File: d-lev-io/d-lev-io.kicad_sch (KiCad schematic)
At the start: 29 parts, among them J1 PJ-059A, J2 USB_C_Receptacle_USB2.0, J8 Conn_01x12_MountingPin, U1 AMS1117-ADJ

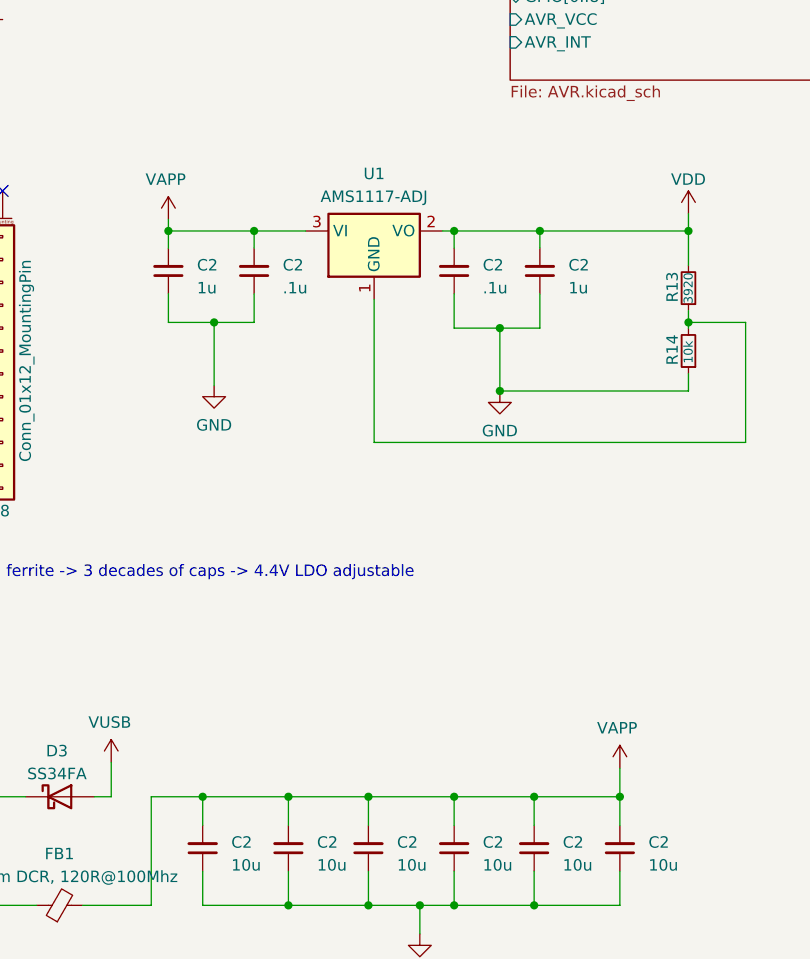
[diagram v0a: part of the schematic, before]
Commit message: mostly done routing
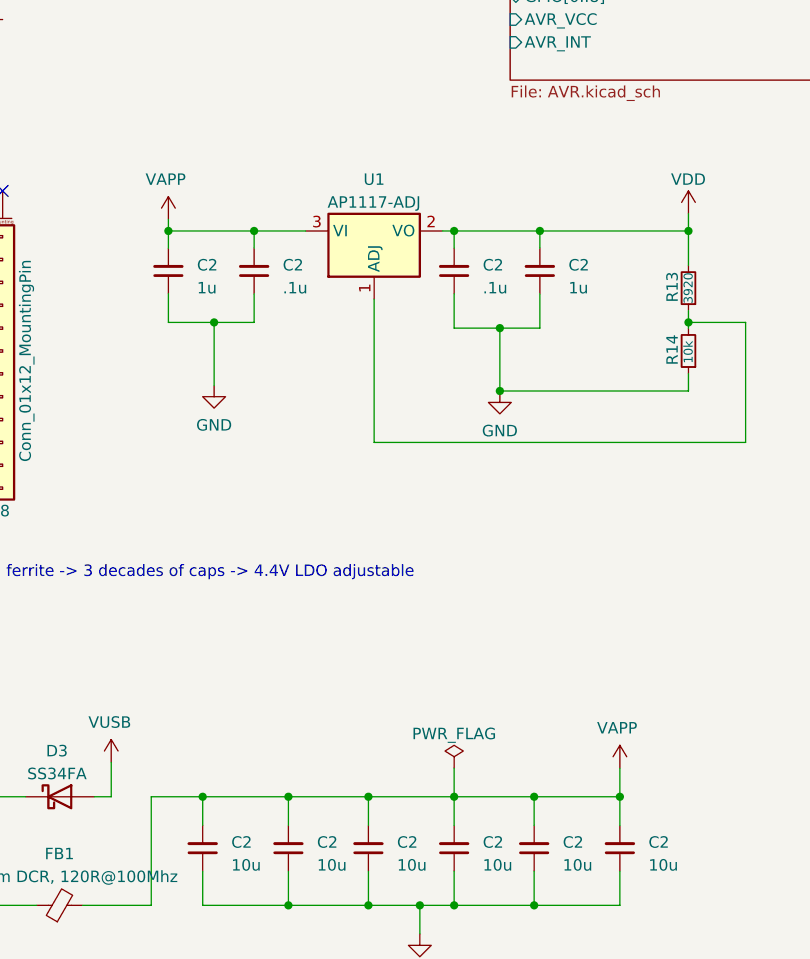
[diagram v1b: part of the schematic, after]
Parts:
- removed U1: AMS1117-ADJ, Package_TO_SOT_SMD:SOT-223-3_TabPin2, symbol Regulator_Linear:AMS1117-5.0
- added U1: AP1117-ADJ, Package_TO_SOT_SMD:SOT-223-3_TabPin2, symbol Regulator_Linear:AP1117-ADJ
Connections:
- net +5V: now also U1.2 (VO)
- net VBUS: now also U1.3 (VI)
- net at R13.1, R14.2: now also U1.1 (ADJ)
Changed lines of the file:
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@@
-    (stroke (width 0) (type default))
-  )
-  (wire (pts (xy 92.075 172.72) (xy 100.965 172.72))
     (stroke (width 0) (type default))
   )
@@
     (stroke (width 0) (type default))
   )
+  (wire (pts (xy 92.075 172.72) (xy 100.965 172.72))
+    (stroke (width 0) (type default))
+  )
   (polyline (pts (xy 111.76 -11.176) (xy 113.03 -12.446))
     (stroke (width 0) (type default))
@@
   )
   (polyline (pts (xy 191.135 -13.97) (xy 191.135 -34.29))
+    (stroke (width 0) (type default))
+  )
+  (wire (pts (xy 92.075 169.545) (xy 92.075 172.72))
     (stroke (width 0) (type default))
   )
@@
     )
   )
+  (symbol (lib_id "Regulator_Linear:AP1117-ADJ") (at 83.185 109.855 0) (unit 1)
+    (in_bom yes) (on_board yes) (dnp no) (fields_autoplaced)
+    (property "Reference" "U1" (at 83.185 104.14 0)
+      (effects (font (size 1.27 1.27)))
+    )
+    (property "Value" "AP1117-ADJ" (at 83.185 106.68 0)
+      (effects (font (size 1.27 1.27)))
+    )
+    (property "Footprint" "Package_TO_SOT_SMD:SOT-223-3_TabPin2" (at 83.185 104.775 0)
+      (effects (font (size 1.27 1.27)) hide)
+    )
+    (property "Datasheet" "http://www.diodes.com/datasheets/AP1117.pdf" (at 85.725 116.205 0)
+      (effects (font (size 1.27 1.27)) hide)
+    )
+    (pin "1")
+    (pin "2")
+    (pin "3")
+    (instances
+      (project "d-lev-io"
+        (path "/9261a07b-ae4a-4d72-8042-ea097cd0e5ed"
+          (reference "U1") (unit 1)
+        )
+      )
+    )
+  )
   (symbol (lib_id "power:VBUS") (at 53.975 168.91 0) (unit 1)
     (in_bom yes) (on_board yes) (dnp no)
@@
         (path "/eb5e8bfd-9871-4528-bf57-58851bf63907/6062d07e-a4ed-44ac-a6b0-014aac464169"
           (reference "#PWR0141") (unit 1)
+        )
+      )
+    )
+  )
+  (symbol (lib_id "power:PWR_FLAG") (at 92.075 169.545 0) (unit 1)
+    (in_bom yes) (on_board yes) (dnp no) (fields_autoplaced)
+    (property "Reference" "#FLG01" (at 92.075 167.64 0)
+      (effects (font (size 1.27 1.27)) hide)
+    )
+    (property "Value" "PWR_FLAG" (at 92.075 165.735 0)
+      (effects (font (size 1.27 1.27)))
+    )
+    (property "Footprint" "" (at 92.075 169.545 0)
+      (effects (font (size 1.27 1.27)) hide)
+    )
+    (property "Datasheet" "~" (at 92.075 169.545 0)
+      (effects (font (size 1.27 1.27)) hide)
+    )
+    (pin "1")
+    (instances
+      (project "d-lev-io"
+        (path "/9261a07b-ae4a-4d72-8042-ea097cd0e5ed"
+          (reference "#FLG01") (unit 1)
         )
       )
@@
         )
       )
-    )
-  )
-  (symbol (lib_name "AMS1117-5.0_1") (lib_id "Regulator_Linear:AMS1117-5.0") (at 83.185 109.855 0) (unit 1)
-    (in_bom yes) (on_board yes) (dnp no) (fields_autoplaced)
-    (property "Reference" "U1" (at 83.185 103.505 0)
-      (effects (font (size 1.27 1.27)))
-    )
-    (property "Value" "AMS1117-ADJ" (at 83.185 106.045 0)
-      (effects (font (size 1.27 1.27)))
-    )
-    (property "Footprint" "Package_TO_SOT_SMD:SOT-223-3_TabPin2" (at 83.185 104.775 0)
-      (effects (font (size 1.27 1.27)) hide)
-    )
-    (property "Datasheet" "http://ams-semitech.com/attachments/File/AMS1117_20120314.pdf" (at 85.725 116.205 0)
-      (effects (font (size 1.27 1.27)) hide)
-    )
-    (pin "1")
-    (pin "2")
-    (pin "3")
-    (instances
-      (project "d-lev-io"
-        (path "/9261a07b-ae4a-4d72-8042-ea097cd0e5ed"
-          (reference "U1") (unit 1)
-        )
-      )

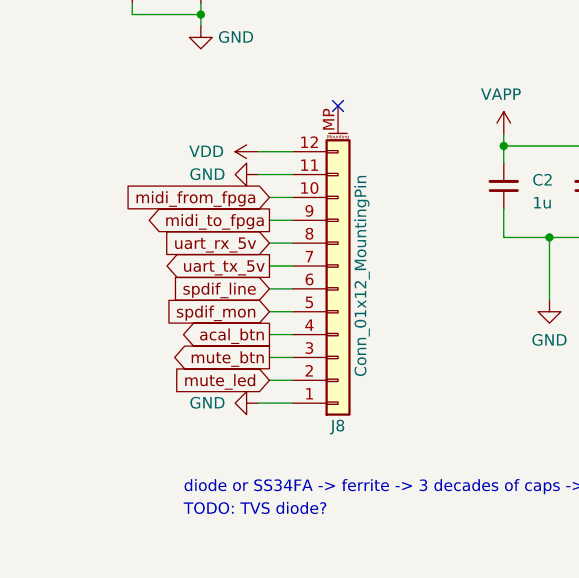
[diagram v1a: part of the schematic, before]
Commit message: Improve routing and rearrange I/O connector
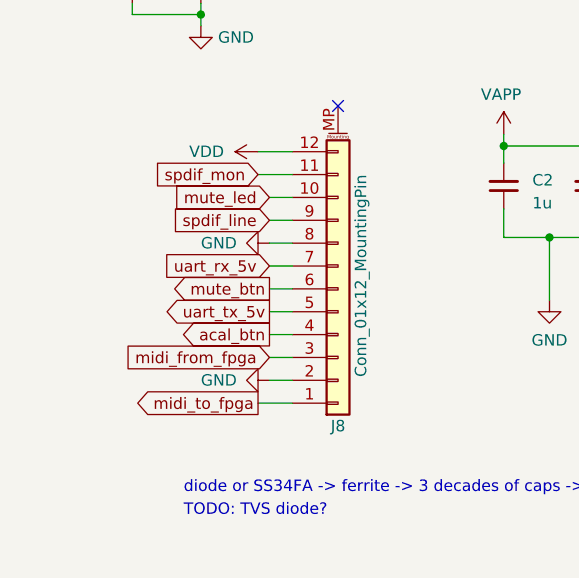
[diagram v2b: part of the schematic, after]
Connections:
- net GND: now also J8.2 (Pin_2), J8.8 (Pin_8); no longer J8.1 (Pin_1), J8.11 (Pin_11)
- net midi_from_fpga: now also J8.3 (Pin_3); no longer J8.10 (Pin_10)
- net midi_to_fpga: now also J8.1 (Pin_1); no longer J8.9 (Pin_9)
- net mute_btn: now also J8.6 (Pin_6); no longer J8.3 (Pin_3)
- net mute_led: now also J8.10 (Pin_10); no longer J8.2 (Pin_2)
- net spdif_line: now also J8.9 (Pin_9); no longer J8.6 (Pin_6)
- net spdif_mon: now also J8.11 (Pin_11); no longer J8.5 (Pin_5)
- net uart_rx_5v: now also J8.7 (Pin_7); no longer J8.8 (Pin_8)
- net uart_tx_5v: now also J8.5 (Pin_5); no longer J8.7 (Pin_7)
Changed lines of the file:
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@@
     )
   )
-  (global_label "spdif_mon" (shape input) (at 34.29 128.27 180) (fields_autoplaced)
+  (global_label "spdif_mon" (shape input) (at 33.02 113.03 180) (fields_autoplaced)
     (effects (font (size 1.27 1.27)) (justify right))
     (property "Intersheetrefs" "${INTERSHEET_REFS}" (at 21.7687 128.27 0)
@@
     )
   )
-  (global_label "spdif_line" (shape input) (at 34.29 125.73 180) (fields_autoplaced)
+  (global_label "spdif_line" (shape input) (at 34.29 118.11 180) (fields_autoplaced)
     (effects (font (size 1.27 1.27)) (justify right))
     (property "Intersheetrefs" "${INTERSHEET_REFS}" (at 22.2524 125.73 0)
@@
     )
   )
-  (global_label "midi_to_fpga" (shape output) (at 34.29 118.11 180) (fields_autoplaced)
+  (global_label "midi_to_fpga" (shape output) (at 33.02 138.43 180) (fields_autoplaced)
     (effects (font (size 1.27 1.27)) (justify right))
     (property "Intersheetrefs" "${INTERSHEET_REFS}" (at 19.3497 123.19 0)
@@
     )
   )
-  (global_label "mute_btn" (shape output) (at 34.29 133.35 180) (fields_autoplaced)
+  (global_label "mute_btn" (shape output) (at 34.29 125.73 180) (fields_autoplaced)
     (effects (font (size 1.27 1.27)) (justify right))
     (property "Intersheetrefs" "${INTERSHEET_REFS}" (at 22.7363 133.35 0)
@@
     )
   )
-  (global_label "uart_tx_5v" (shape output) (at 34.29 123.19 180) (fields_autoplaced)
+  (global_label "uart_tx_5v" (shape output) (at 34.29 128.27 180) (fields_autoplaced)
     (effects (font (size 1.27 1.27)) (justify right))
     (property "Intersheetrefs" "${INTERSHEET_REFS}" (at 21.7082 118.11 0)
@@
     )
   )
-  (global_label "uart_rx_5v" (shape input) (at 34.29 120.65 180) (fields_autoplaced)
+  (global_label "uart_rx_5v" (shape input) (at 34.29 123.19 180) (fields_autoplaced)
     (effects (font (size 1.27 1.27)) (justify right))
     (property "Intersheetrefs" "${INTERSHEET_REFS}" (at 21.6477 115.57 0)
@@
     )
   )
-  (global_label "midi_from_fpga" (shape input) (at 34.29 115.57 180) (fields_autoplaced)
+  (global_label "midi_from_fpga" (shape input) (at 34.29 133.35 180) (fields_autoplaced)
     (effects (font (size 1.27 1.27)) (justify right))
     (property "Intersheetrefs" "${INTERSHEET_REFS}" (at 16.8702 120.65 0)
@@
     )
   )
-  (global_label "mute_led" (shape input) (at 34.29 135.89 180) (fields_autoplaced)
+  (global_label "mute_led" (shape input) (at 34.29 115.57 180) (fields_autoplaced)
     (effects (font (size 1.27 1.27)) (justify right))
     (property "Intersheetrefs" "${INTERSHEET_REFS}" (at 22.8572 135.89 0)
@@
     )
   )
-  (symbol (lib_id "power:GND") (at 33.02 113.03 270) (unit 1)
-    (in_bom yes) (on_board yes) (dnp no)
-    (property "Reference" "#PWR020" (at 26.67 113.03 0)
-      (effects (font (size 1.27 1.27)) hide)
-    )
-    (property "Value" "GND" (at 25.4 113.03 90)
+  (symbol (lib_id "power:GND") (at 34.29 135.89 270) (unit 1)
+    (in_bom yes) (on_board yes) (dnp no)
+    (property "Reference" "#PWR020" (at 27.94 135.89 0)
+      (effects (font (size 1.27 1.27)) hide)
+    )
+    (property "Value" "GND" (at 26.67 135.89 90)
       (effects (font (size 1.27 1.27)) (justify left))
     )
-    (property "Footprint" "" (at 33.02 113.03 0)
-      (effects (font (size 1.27 1.27)) hide)
-    )
-    (property "Datasheet" "" (at 33.02 113.03 0)
+    (property "Footprint" "" (at 34.29 135.89 0)
+      (effects (font (size 1.27 1.27)) hide)
+    )
+    (property "Datasheet" "" (at 34.29 135.89 0)
       (effects (font (size 1.27 1.27)) hide)
     )
@@
     )
   )
-  (symbol (lib_id "power:GND") (at 33.02 138.43 270) (unit 1)
-    (in_bom yes) (on_board yes) (dnp no)
-    (property "Reference" "#PWR021" (at 26.67 138.43 0)
-      (effects (font (size 1.27 1.27)) hide)
-    )
-    (property "Value" "GND" (at 25.4 138.43 90)
+  (symbol (lib_id "power:GND") (at 34.29 120.65 270) (unit 1)
+    (in_bom yes) (on_board yes) (dnp no)
+    (property "Reference" "#PWR021" (at 27.94 120.65 0)
+      (effects (font (size 1.27 1.27)) hide)
+    )
+    (property "Value" "GND" (at 26.67 120.65 90)
       (effects (font (size 1.27 1.27)) (justify left))
     )
-    (property "Footprint" "" (at 33.02 138.43 0)
-      (effects (font (size 1.27 1.27)) hide)
-    )
-    (property "Datasheet" "" (at 33.02 138.43 0)
-      (effects (font (size 1.27 1.27)) hide)
-    )
+    (property "Footprint" "" (at 34.29 120.65 0)
+      (effects (font (size 1.27 1.27)) hide)
+    )
+    (property "Datasheet" "" (at 34.29 120.65 0)
+      (effects (font (size 1.27 1.27)) hide)
+    )
